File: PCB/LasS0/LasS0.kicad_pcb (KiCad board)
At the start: 2 copper layers, 29.3 x 82 mm, 38 parts, among them J1 CiKe2PinSock, J2 CiKe2PinSock, J3 CiKe2PinSock, J4 CiKe2PinSock, Q1 S8050, Q2 S8050, U1 TPS54331D, U2 EL817S1

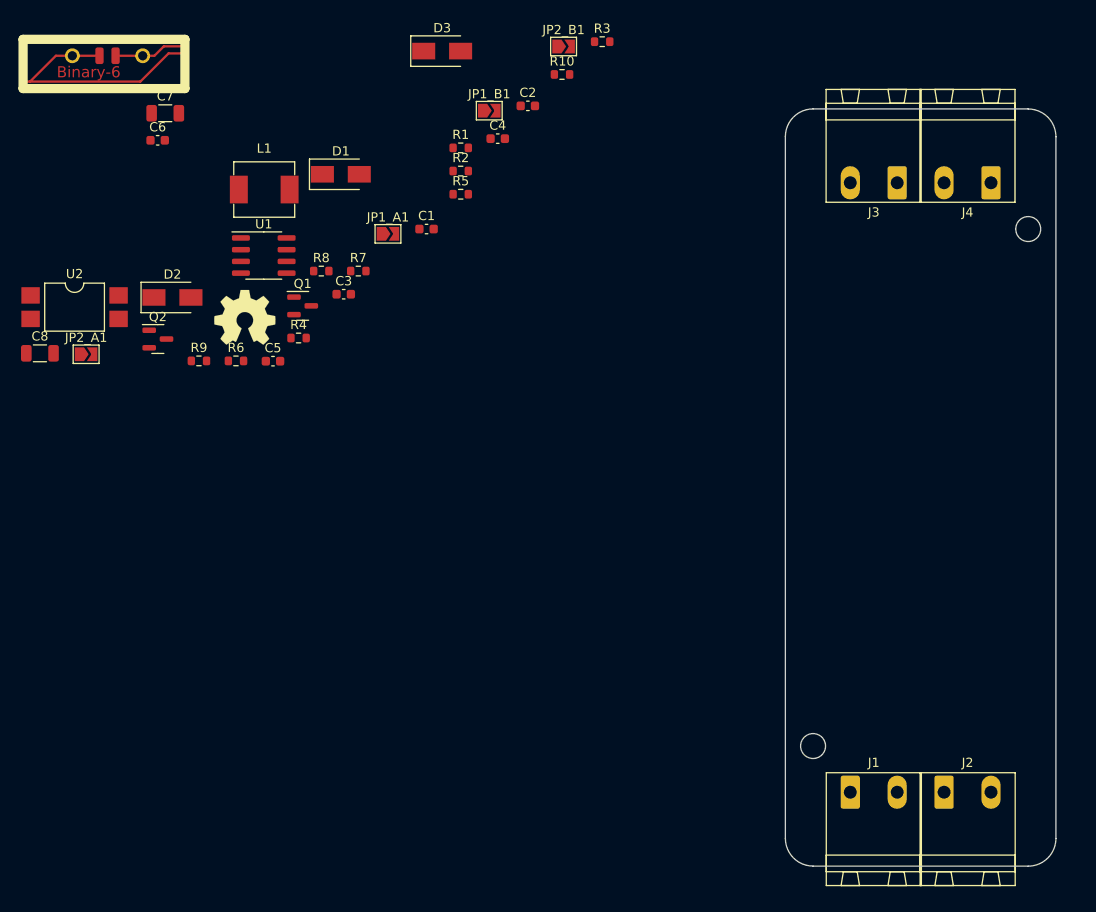
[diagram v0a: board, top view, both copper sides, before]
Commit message: Route PCB initial version
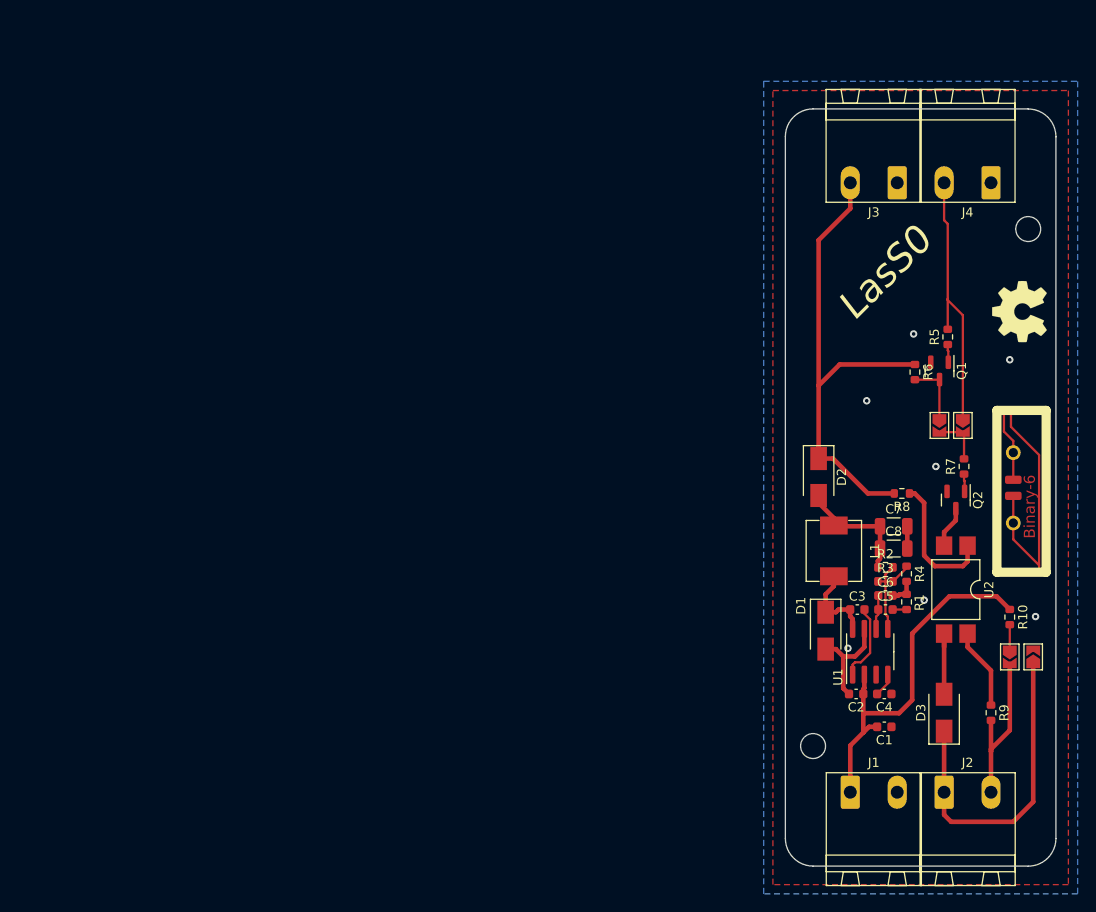
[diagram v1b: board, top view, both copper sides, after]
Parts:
- moved LOGO1 109.1 mm to (159.5, 100.0), turned to 90 degrees
- moved JP2_A1 105.3 mm to (158.2, 118.3), turned to -90 degrees
- moved U2 100.2 mm to (152.3, 111.0), turned to -90 degrees
- moved C8 94.8 mm to (145.6, 106.6)
- moved R9 93.9 mm to (156.1, 124.4), turned to -90 degrees
- moved C6 93.0 mm to (144.7, 111.7)
- moved C7 90.7 mm to (145.6, 104.2)
- moved D3 89.9 mm to (151.1, 124.4), turned to 90 degrees
- moved Q2 88.2 mm to (152.3, 101.3), turned to -90 degrees
- moved LOGO3 83.9 mm to (159.2, 81.0), turned to 90 degrees
- moved JP2_B1 83.4 mm to (160.7, 118.3), turned to 90 degrees
- moved U1 78.5 mm to (143.0, 117.8), turned to 90 degrees
- moved R10 76.2 mm to (158.2, 114.0), turned to -90 degrees
- moved R6 73.5 mm to (147.9, 87.5), turned to -90 degrees
- moved C4 73.3 mm to (144.6, 122.4)
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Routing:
- net +5V: track 0.00 -> 52.4 mm
- net VCC: track 0.00 -> 41.0 mm
- net /S0-: track 0.00 -> 34.9 mm
- net /D0: track 0.00 -> 29.7 mm
- net /S0+: track 0.00 -> 18.1 mm
- net GND: track 0.00 -> 16.6 mm, vias 0 -> 7
- net Net-(R8-Pad1): track 0.00 -> 14.8 mm
- net Net-(C7-Pad1): track 0.00 -> 13.5 mm
- net Net-(C3-Pad1): track 0.00 -> 9.23 mm
- net Net-(R9-Pad1): track 0.00 -> 8.80 mm
- net Net-(C3-Pad2): track 0.00 -> 8.46 mm
- net Net-(D3-Pad2): track 0.00 -> 8.03 mm
- net Net-(R2-Pad2): track 0.00 -> 7.98 mm
- net Net-(JP1_B1-Pad1): track 0.00 -> 6.90 mm
- net Net-(JP1_A1-Pad2): track 0.00 -> 5.55 mm
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- added copper zone on B.Cu, net GND
- added copper zone on F.Cu, net GND
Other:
- board text added: "LasS0"

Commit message: Prettify PCB
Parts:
- moved LOGO3 5.07 mm to (158.2, 85.9), turned to 0 degrees
- moved D3 2.80 mm to (151.2, 121.6)
- moved R9 2.79 mm to (156.1, 121.6)
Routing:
- net /S0-: track 34.9 -> 37.7 mm
- net /S0+: track 18.1 -> 20.9 mm
- net Net-(R9-Pad1): track 8.80 -> 6.00 mm
- net Net-(D3-Pad2): track 8.03 -> 5.29 mm
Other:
- board text added: "+5V"
- board text added: "Choose one: Direct Output Inverted Output"
- board text added: "D0"
- board text added: "GND"
- board text added: "Logic level impulse to S0 converter Chrismettal 2021_06 github.com/Chrismettal/LasS0"
- board text added: "NC"
- board text added: "S0+"
- board text added: "S0-"
- board text added: "Set both for pullup to VCC on S0+"
- board text added: "VCC"

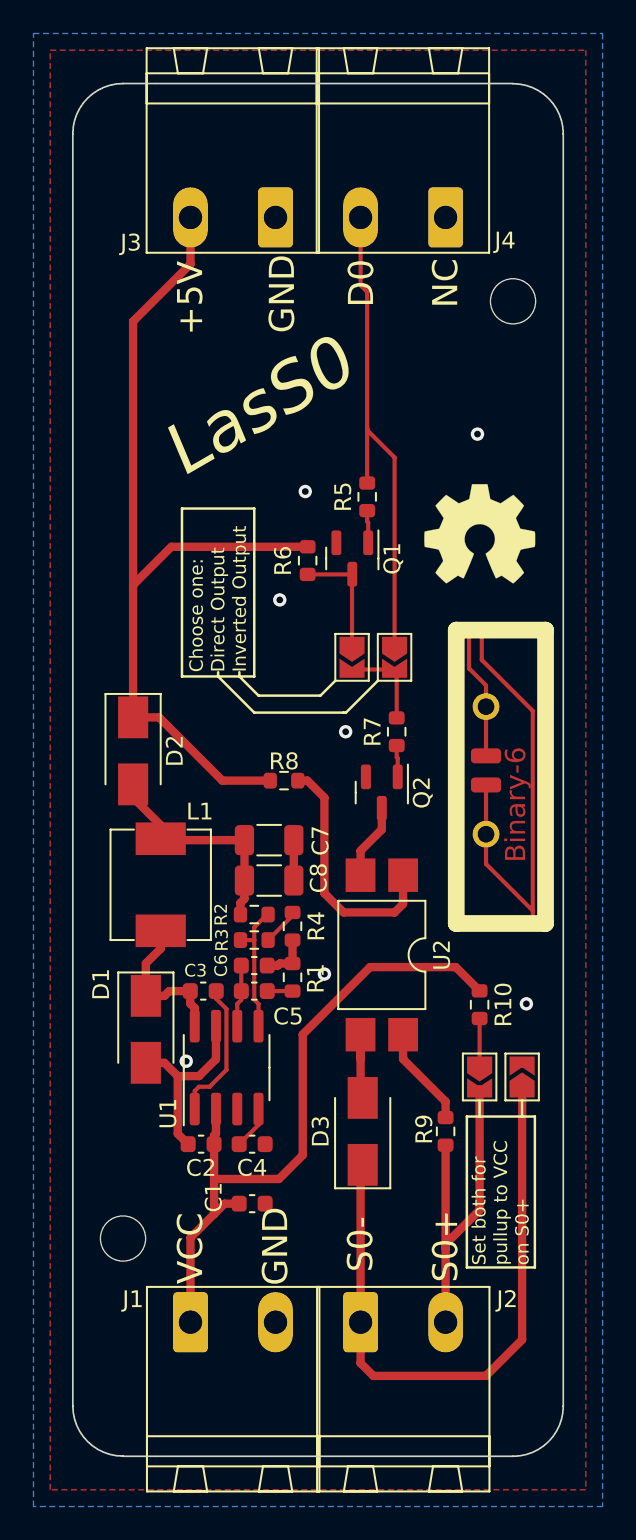
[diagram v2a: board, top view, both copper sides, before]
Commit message: Clear up DRC fails
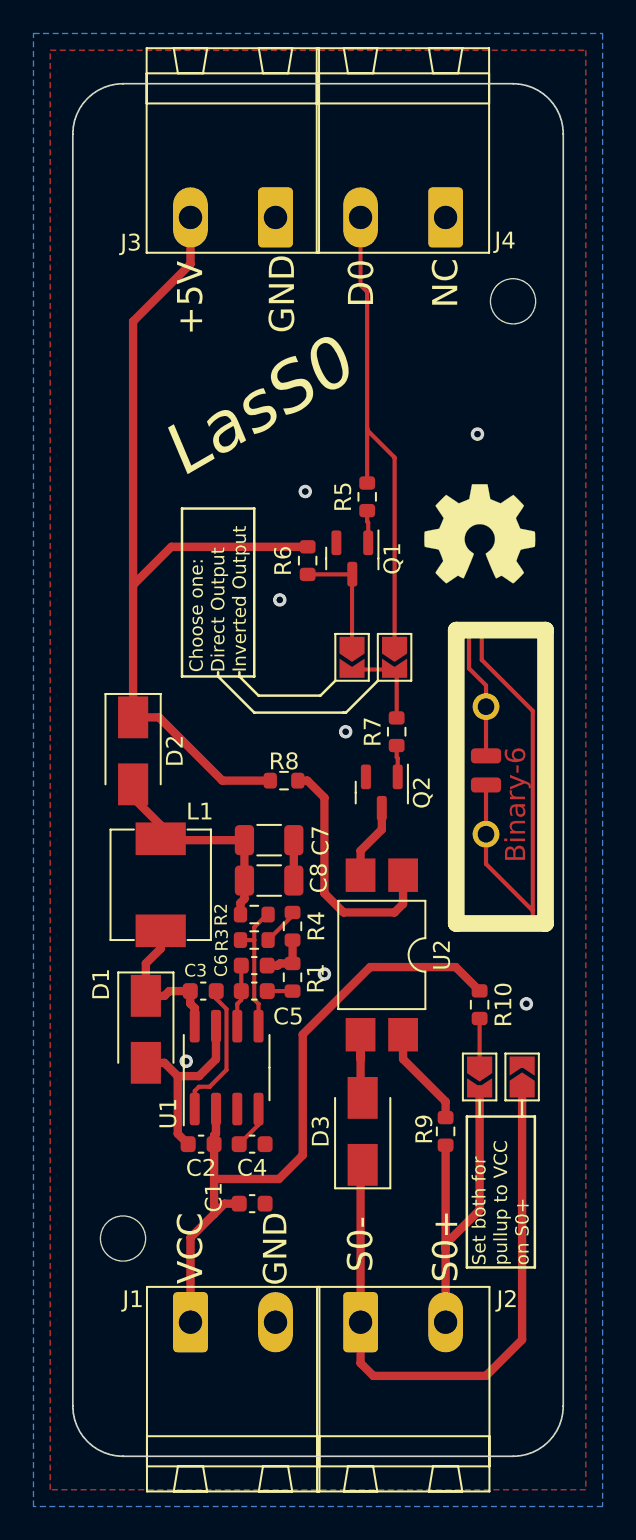
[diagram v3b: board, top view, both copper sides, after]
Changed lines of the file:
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@@
     )
     (pad_to_mask_clearance 0)
-    (grid_origin 148.51 100)
+    (grid_origin 133.86 138)
     (pcbplotparams
       (layerselection 0x00010fc_ffffffff)
@@
   (gr_circle (center 148.51 100) (end 148.66 100) (layer "Eco1.User") (width 0.15) (fill none))
   (gr_line (start 148.51 56.6) (end 148.51 143.5) (layer "Eco1.User") (width 0.15))
+  (gr_arc (start 136.86 62) (end 133.86 62) (angle 90) (layer "Edge.Cuts") (width 0.1))
+  (gr_line (start 163.16 138) (end 163.16 62) (layer "Edge.Cuts") (width 0.1))
   (gr_arc (start 160.16 62) (end 160.16 59) (angle 90) (layer "Edge.Cuts") (width 0.1))
-  (gr_line (start 160.16 141) (end 136.86 141) (layer "Edge.Cuts") (width 0.1))
-  (gr_arc (start 136.86 61.99) (end 133.86 61.99) (angle 90) (layer "Edge.Cuts") (width 0.1))
-  (gr_line (start 163.16 62) (end 163.16 138) (layer "Edge.Cuts") (width 0.1))
-  (gr_line (start 133.86 137.99) (end 133.86 61.99) (layer "Edge.Cuts") (width 0.1))
-  (gr_line (start 136.86 58.99) (end 160.16 58.99) (layer "Edge.Cuts") (width 0.1))
+  (gr_line (start 133.86 62) (end 133.86 138) (layer "Edge.Cuts") (width 0.1))
+  (gr_arc (start 136.86 138) (end 133.86 138) (angle -90) (layer "Edge.Cuts") (width 0.1))
   (gr_arc (start 160.16 138) (end 163.16 138) (angle 90) (layer "Edge.Cuts") (width 0.1))
-  (gr_arc (start 136.86 137.99) (end 136.86 140.99) (angle 90) (layer "Edge.Cuts") (width 0.1))
+  (gr_line (start 160.16 59) (end 136.86 59) (layer "Edge.Cuts") (width 0.1))
+  (gr_line (start 136.86 141) (end 160.16 141) (layer "Edge.Cuts") (width 0.1))
   (gr_text "LasS0" (at 139.62 100 90) (layer "B.SilkS")
     (effects (font (size 3 3) (thickness 0.75) italic) (justify mirror))
@@
     (effects (font (size 1.5 1.5) (thickness 0.25)))
   )
-  (gr_text "GND" (at 145.97 128.448 90) (layer "F.SilkS")
-    (effects (font (size 1.5 1.5) (thickness 0.25)))
+  (gr_text "GND" (at 145.97 128.602 90) (layer "F.SilkS")
+    (effects (font (size 1.4 1.4) (thickness 0.25)))
   )
   (gr_text "S0-" (at 151.05 128.321 90) (layer "F.SilkS")

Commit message: Minor cleanup and add JLC number
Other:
- board text added: "HASH"
- board text added: "JLCJLCJLCJLC"
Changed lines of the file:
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@@
   )
   (paper "A4")
+  (title_block
+    (title "LasS0")
+    (date "2021-06-03")
+    (rev "v0.1")
+  )
   (layers
     (0 "F.Cu" signal)
@@
     (effects (font (size 2 2) (thickness 0.3)) (justify mirror))
   )
+  (gr_text "JLCJLCJLCJLC" (at 161.8 132.666 90) (layer "B.SilkS")
+    (effects (font (size 1 1) (thickness 0.15)) (justify mirror))
+  )
   (gr_text "GND" (at 146.3764 71.552 90) (layer "F.SilkS")
     (effects (font (size 1.5 1.5) (thickness 0.25)))
@@
     (effects (font (size 1.5 1.5) (thickness 0.25)))
   )
+  (gr_text "HASH" (at 160.276 64.594 90) (layer "F.SilkS")
+    (effects (font (size 1 1) (thickness 0.15)))
+  )
   (gr_text "GND" (at 145.97 128.602 90) (layer "F.SilkS")

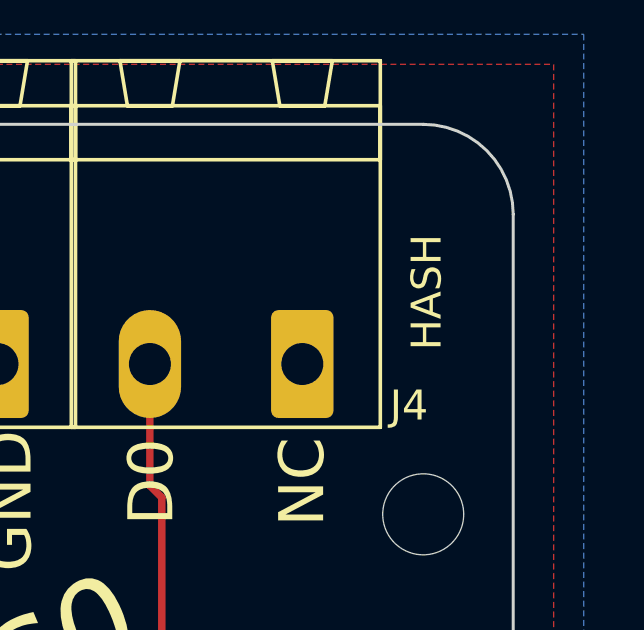
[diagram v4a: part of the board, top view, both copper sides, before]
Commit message: Add version hash to silkscreen
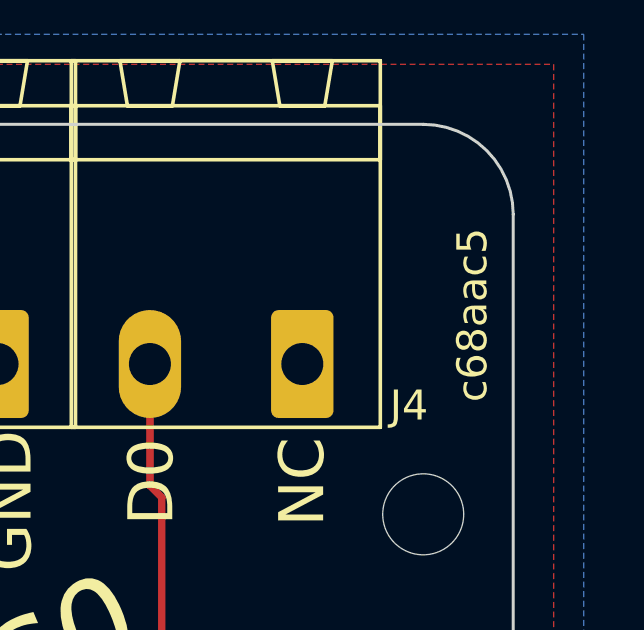
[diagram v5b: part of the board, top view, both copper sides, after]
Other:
- board text added: "c68aac5"
- board text removed: "HASH"
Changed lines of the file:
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@@
     (effects (font (size 1.5 1.5) (thickness 0.25)))
   )
-  (gr_text "HASH" (at 160.276 64.594 90) (layer "F.SilkS")
+  (gr_text "c68aac5" (at 161.8 65.356 90) (layer "F.SilkS")
     (effects (font (size 1 1) (thickness 0.15)))
   )

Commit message: Update version hash
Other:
- board text added: "f7945a1"
- board text removed: "c68aac5"
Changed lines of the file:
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@@
     (effects (font (size 1.5 1.5) (thickness 0.25)))
   )
-  (gr_text "c68aac5" (at 161.8 65.356 90) (layer "F.SilkS")
+  (gr_text "f7945a1" (at 161.8 64.848 90) (layer "F.SilkS")
     (effects (font (size 1 1) (thickness 0.15)))
   )

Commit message: Update version hash
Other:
- board text added: "38b7723"
- board text removed: "f7945a1"
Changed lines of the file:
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@@
     (effects (font (size 1.5 1.5) (thickness 0.25)))
   )
-  (gr_text "f7945a1" (at 161.8 64.848 90) (layer "F.SilkS")
+  (gr_text "38b7723\n" (at 161.8 64.848 90) (layer "F.SilkS")
     (effects (font (size 1 1) (thickness 0.15)))
   )
